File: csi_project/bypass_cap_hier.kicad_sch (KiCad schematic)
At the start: 6 parts

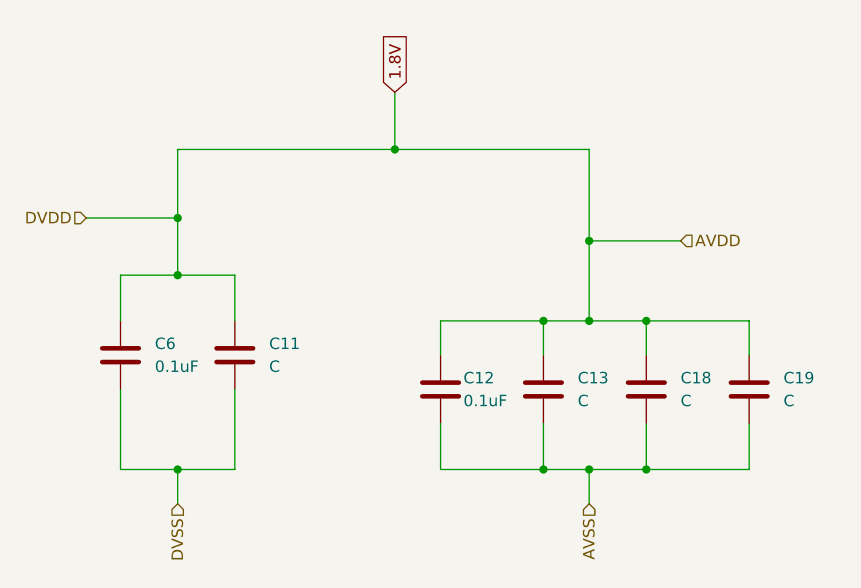
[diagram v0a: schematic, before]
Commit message: Changed the value of a R and a few Cs
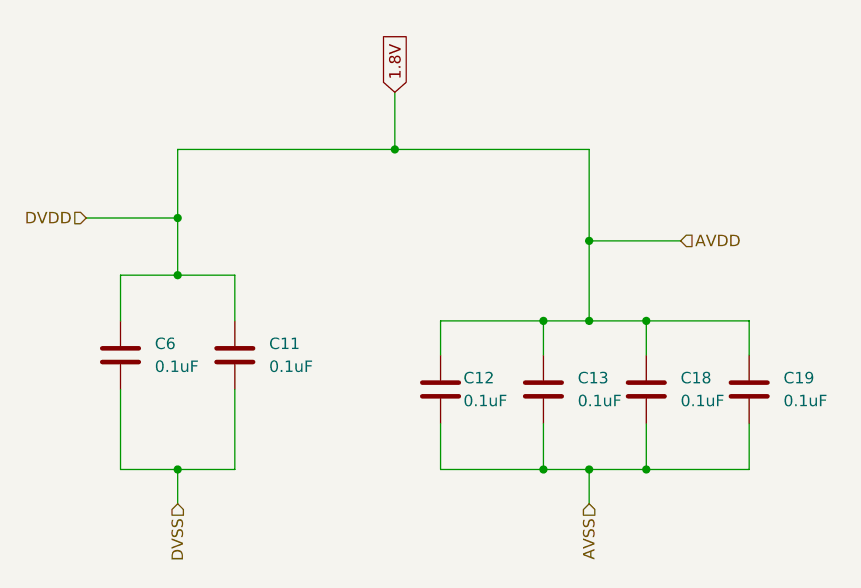
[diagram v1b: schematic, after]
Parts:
- C11, C13, C18, C19: value C -> 0.1uF
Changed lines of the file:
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@@
 			)
 		)
-		(property "Value" "C"
+		(property "Value" "0.1uF"
 			(at 195.58 82.5499 0)
 			(effects
@@
 			)
 		)
-		(property "Value" "C"
+		(property "Value" "0.1uF"
 			(at 138.43 78.7399 0)
 			(effects
@@
 			)
 		)
-		(property "Value" "C"
+		(property "Value" "0.1uF"
 			(at 172.72 82.5499 0)
 			(effects
@@
 			)
 		)
-		(property "Value" "C"
+		(property "Value" "0.1uF"
 			(at 184.15 82.5499 0)
 			(effects

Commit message: Imported custom capacitor and resistor symbols and footprints, and assigned them accordingly.
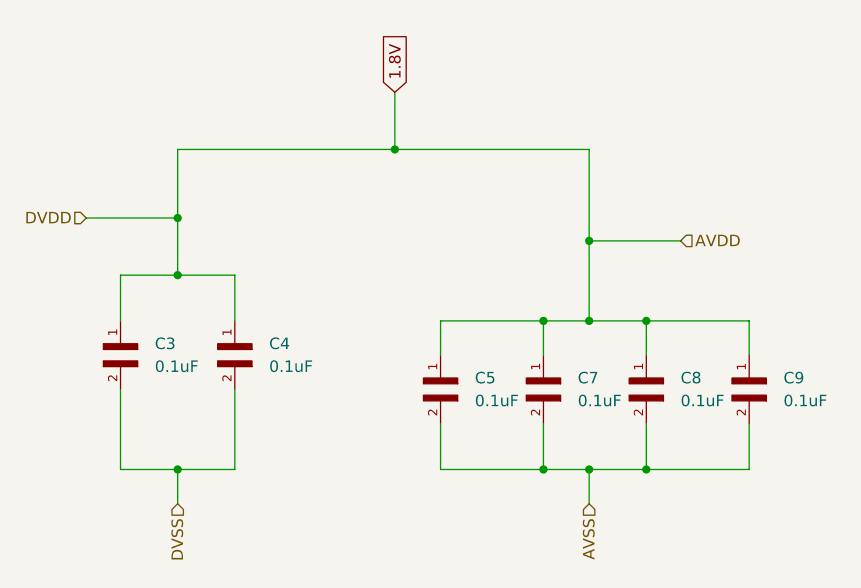
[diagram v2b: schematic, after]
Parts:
- removed C11, C12, C13, C18, C19, C6: 0.1uF, symbol Device:C
- added C3, C4, C5, C7, C8, C9: 0.1uF, Custom Caps n Res:CL05B104KP5NNNC, symbol Custom Caps n Res:CL05B104KP5NNNC
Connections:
- net 1.8V: now also C3.1, C4.1, C5.1, C7.1, C8.1, C9.1
- net AVSS: now also C5.2, C7.2, C8.2, C9.2
- net DVSS: now also C3.2, C4.2
